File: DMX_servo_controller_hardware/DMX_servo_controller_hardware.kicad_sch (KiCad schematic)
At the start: 21 parts

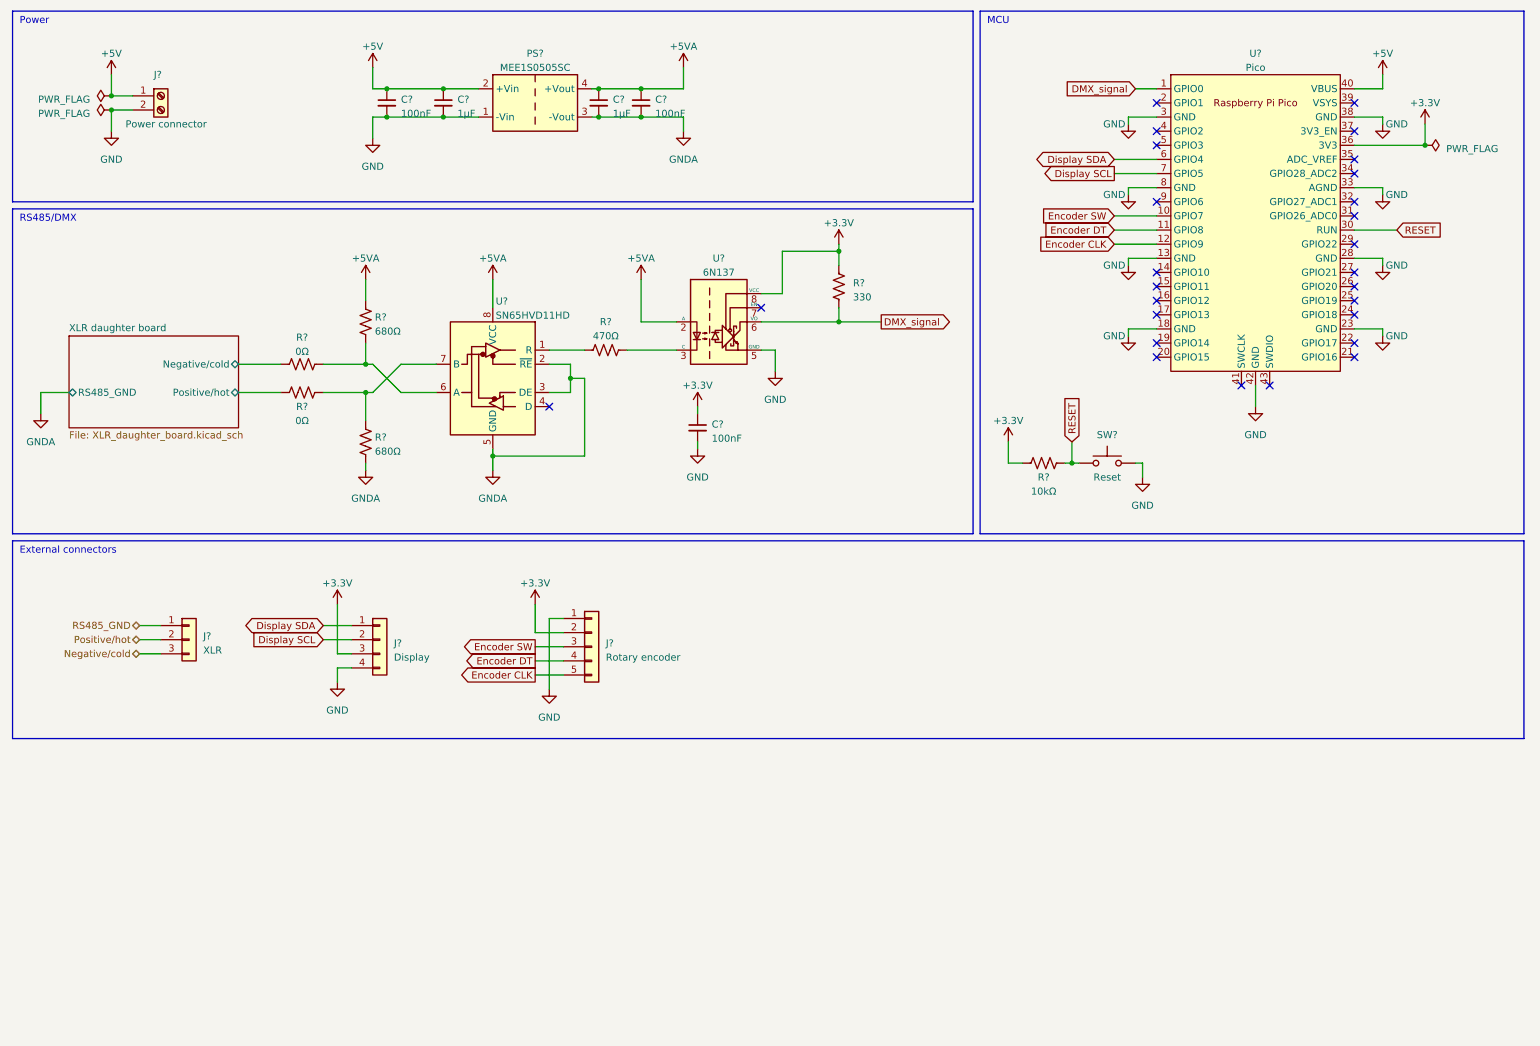
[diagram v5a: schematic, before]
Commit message: WIP: Adds PCA9685 PWM driver
This adds the IC and some minimal circuitry around it, but there's still
work to be done here.
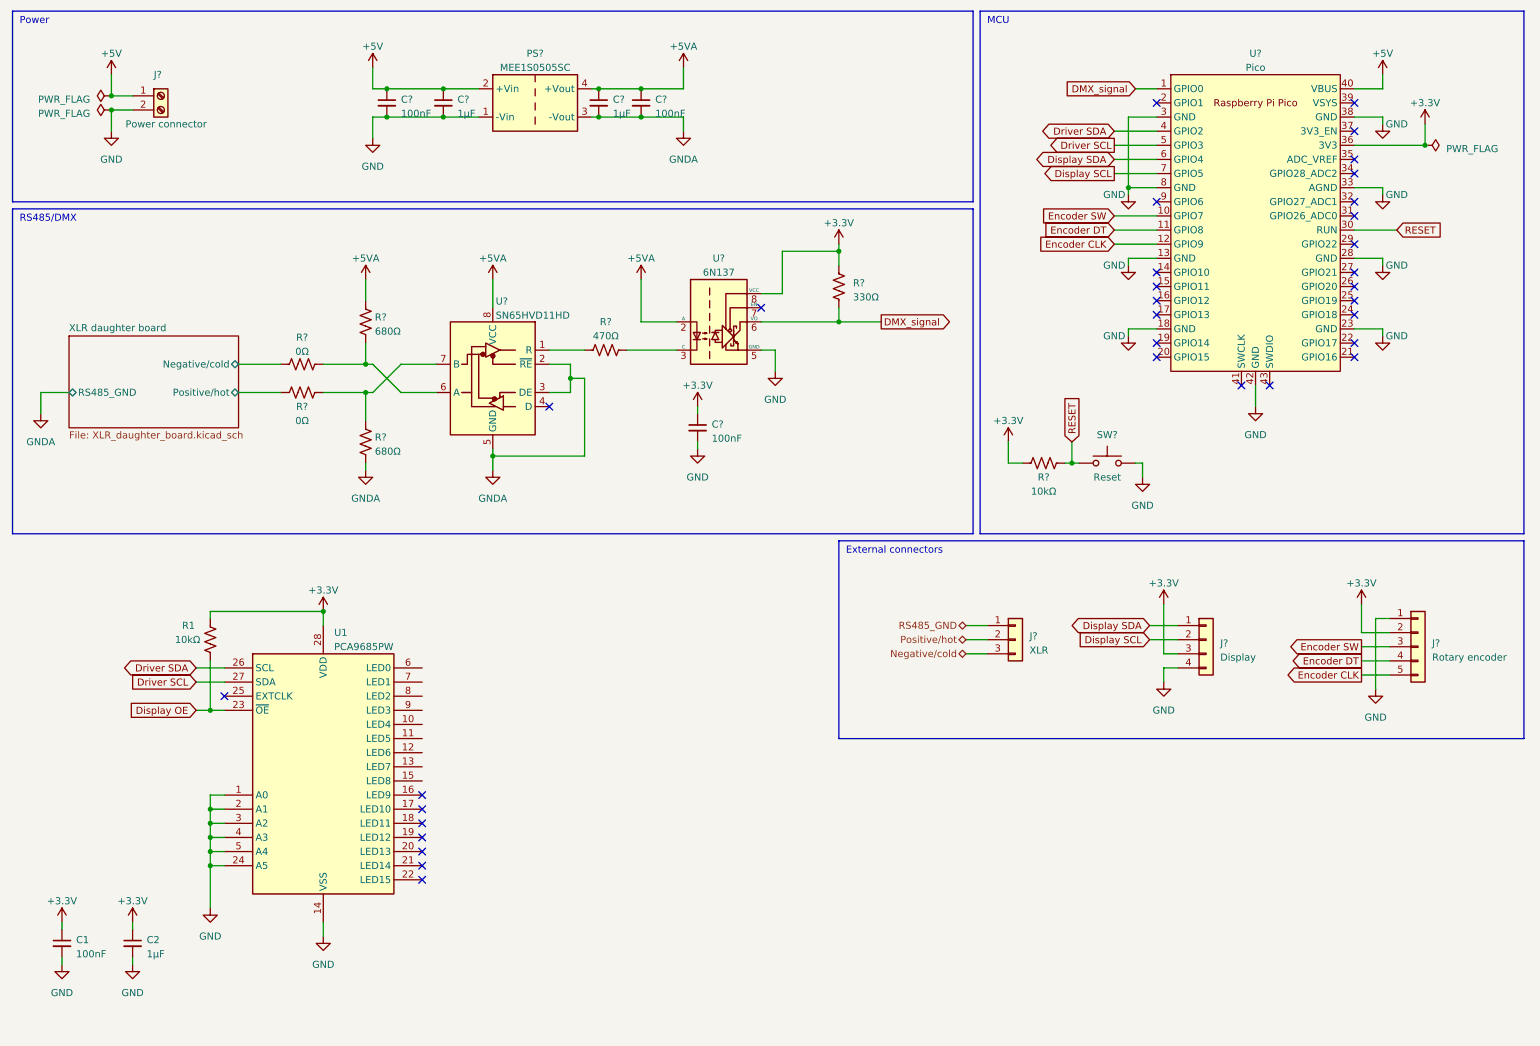
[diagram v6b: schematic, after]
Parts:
- added C1: 100nF, symbol Device:C_Small
- added C2: 1μF, symbol Device:C_Small
- added R1: 10kΩ, symbol Device:R_US
- added U1: PCA9685PW, Package_SO:TSSOP-28_4.4x9.7mm_P0.65mm, symbol Driver_LED:PCA9685PW
- R?: value 330 -> 330Ω
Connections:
- net +3.3V: now also C1.1, C2.1, R1.1, U1.28 (VDD)
- net GND: now also C1.2, C2.2, U1.1 (A0), U1.14 (VSS), U1.2 (A1), U1.24 (A5), U1.3 (A2), U1.4 (A3), U1.5 (A4)
- net Driver SDA: now reaches U?.4 (GPIO2)
- net Driver SDA: now also U1.26 (SCL)
- net Driver SCL: now reaches U?.5 (GPIO3)
- net Driver SCL: now also U1.27 (SDA)
- new net Display OE: R1.2, U1.23 (~{OE})
- no-connect marks 27 -> 33
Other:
- moved on the sheet: J?

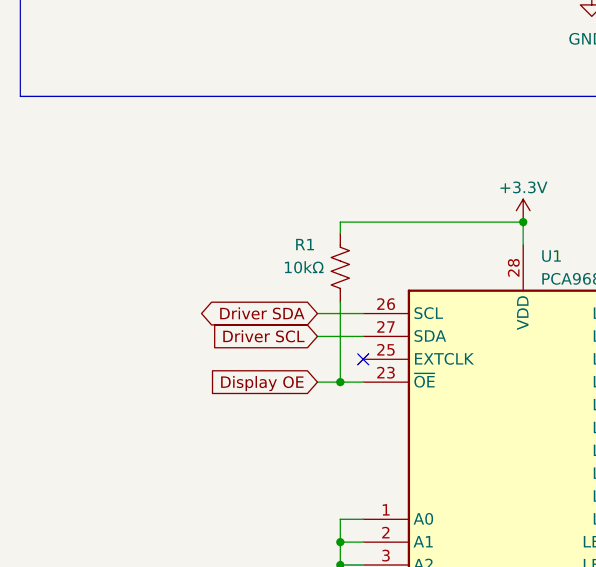
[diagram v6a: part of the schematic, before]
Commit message: Adds pull-up resistors to PCA9685 i2c lines
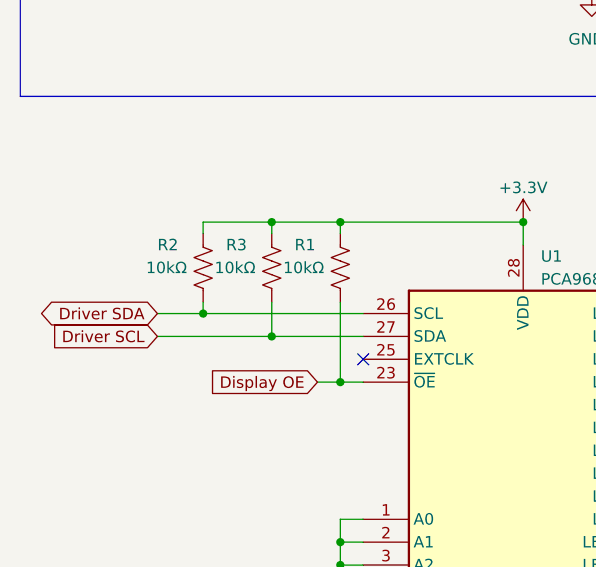
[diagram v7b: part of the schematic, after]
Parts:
- added R2, R3: 10kΩ, symbol Device:R_US
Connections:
- net +3.3V: now also R2.1, R3.1
- net Driver SCL: now also R3.2
- net Driver SDA: now also R2.2
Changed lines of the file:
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@@
   (junction (at 203.2 93.98) (diameter 0) (color 0 0 0 0)
   )
+  (junction (at 48.26 120.65) (diameter 0) (color 0 0 0 0)
+  )
   (junction (at 48.26 138.43) (diameter 0) (color 0 0 0 0)
   )
@@
   (junction (at 48.26 158.75) (diameter 0) (color 0 0 0 0)
   )
+  (junction (at 40.64 120.65) (diameter 0) (color 0 0 0 0)
+  )
   (junction (at 161.29 55.88) (diameter 0) (color 0 0 0 0)
   )
@@
   (junction (at 76.2 76.2) (diameter 0) (color 0 0 0 0)
   )
+  (junction (at 33.02 130.81) (diameter 0) (color 0 0 0 0)
+  )
   (junction (at 48.26 156.21) (diameter 0) (color 0 0 0 0)
   )
@@
   )
   (junction (at 80.01 26.67) (diameter 0) (color 0 0 0 0)
+  )
+  (junction (at 40.64 133.35) (diameter 0) (color 0 0 0 0)
   )
   (junction (at 125.73 26.67) (diameter 0) (color 0 0 0 0)
@@
   (no_connect (at 254 39.37))
   (no_connect (at 218.44 29.21))
+  (wire (pts (xy 40.64 120.65) (xy 48.26 120.65))
+    (stroke (width 0) (type default))
+  )
   (wire (pts (xy 210.82 39.37) (xy 218.44 39.37))
     (stroke (width 0) (type default))
@@
     (stroke (width 0) (type default))
   )
+  (wire (pts (xy 33.02 130.81) (xy 50.8 130.81))
+    (stroke (width 0) (type default))
+  )
   (wire (pts (xy 215.9 93.98) (xy 215.9 96.52))
     (stroke (width 0) (type default))
@@
     (stroke (width 0) (type default))
   )
+  (wire (pts (xy 33.02 130.81) (xy 33.02 129.54))
+    (stroke (width 0) (type default))
+  )
   (wire (pts (xy 210.82 54.61) (xy 218.44 54.61))
     (stroke (width 0) (type default))
@@
     (stroke (width 0) (type default))
   )
-  (wire (pts (xy 45.72 130.81) (xy 50.8 130.81))
+  (wire (pts (xy 27.94 130.81) (xy 33.02 130.81))
     (stroke (width 0) (type default))
   )
@@
     (stroke (width 0) (type default))
   )
+  (wire (pts (xy 33.02 120.65) (xy 40.64 120.65))
+    (stroke (width 0) (type default))
+  )
   (wire (pts (xy 254 69.85) (xy 259.08 69.85))
     (stroke (width 0) (type default))
@@
     (stroke (width 0) (type default))
   )
+  (wire (pts (xy 33.02 121.92) (xy 33.02 120.65))
+    (stroke (width 0) (type default))
+  )
   (wire (pts (xy 82.55 81.28) (xy 88.9 81.28))
     (stroke (width 0) (type default))
@@
     (stroke (width 0) (type default))
   )
-  (wire (pts (xy 45.72 133.35) (xy 50.8 133.35))
+  (wire (pts (xy 40.64 121.92) (xy 40.64 120.65))
+    (stroke (width 0) (type default))
+  )
+  (wire (pts (xy 27.94 133.35) (xy 40.64 133.35))
     (stroke (width 0) (type default))
   )
@@
   )
   (wire (pts (xy 161.29 68.58) (xy 161.29 66.04))
+    (stroke (width 0) (type default))
+  )
+  (wire (pts (xy 40.64 133.35) (xy 50.8 133.35))
+    (stroke (width 0) (type default))
+  )
+  (wire (pts (xy 40.64 129.54) (xy 40.64 133.35))
     (stroke (width 0) (type default))
   )
@@
     )
   )
-  (global_label "Driver SDA" (shape bidirectional) (at 45.72 130.81 180) (fields_autoplaced)
-    (effects (font (size 1.27 1.27)) (justify right))
-    (property "Intersheetrefs" "${INTERSHEET_REFS}" (at 31.6638 130.81 0)
+  (global_label "Driver SDA" (shape bidirectional) (at 27.94 130.81 180) (fields_autoplaced)
+    (effects (font (size 1.27 1.27)) (justify right))
+    (property "Intersheetrefs" "${INTERSHEET_REFS}" (at 13.8838 130.81 0)
       (effects (font (size 1.27 1.27)) (justify right) hide)
     )
@@
     )
   )
-  (global_label "Driver SCL" (shape input) (at 45.72 133.35 180) (fields_autoplaced)
-    (effects (font (size 1.27 1.27)) (justify right))
-    (property "Intersheetrefs" "${INTERSHEET_REFS}" (at 32.8356 133.35 0)
+  (global_label "Driver SCL" (shape input) (at 27.94 133.35 180) (fields_autoplaced)
+    (effects (font (size 1.27 1.27)) (justify right))
+    (property "Intersheetrefs" "${INTERSHEET_REFS}" (at 15.0556 133.35 0)
       (effects (font (size 1.27 1.27)) (justify right) hide)
     )
@@
         (path "/cd90393c-7fb4-4867-84b8-7df1a2bf6613"
           (reference "#PWR?") (unit 1)
+        )
+      )
+    )
+  )
+  (symbol (lib_id "Device:R_US") (at 40.64 125.73 0) (unit 1)
+    (in_bom yes) (on_board yes) (dnp no)
+    (property "Reference" "R3" (at 35.56 123.19 0)
+      (effects (font (size 1.27 1.27)) (justify left))
+    )
+    (property "Value" "10kΩ" (at 34.29 125.73 0)
+      (effects (font (size 1.27 1.27)) (justify left))
+    )
+    (property "Footprint" "" (at 41.656 125.984 90)
+      (effects (font (size 1.27 1.27)) hide)
+    )
+    (property "Datasheet" "~" (at 40.64 125.73 0)
+      (effects (font (size 1.27 1.27)) hide)
+    )
+    (pin "1")
+    (pin "2")
+    (instances
+      (project "DMX_servo_controller_hardware"
+        (path "/cd90393c-7fb4-4867-84b8-7df1a2bf6613"
+          (reference "R3") (unit 1)
         )
       )
@@
         )
       )
+    )
+  )
+  (symbol (lib_id "Device:R_US") (at 33.02 125.73 0) (unit 1)
+    (in_bom yes) (on_board yes) (dnp no)
+    (property "Reference" "R2" (at 27.94 123.19 0)
+      (effects (font (size 1.27 1.27)) (justify left))
+    )
+    (property "Value" "10kΩ" (at 26.67 125.73 0)
+      (effects (font (size 1.27 1.27)) (justify left))
+    )
+    (property "Footprint" "" (at 34.036 125.984 90)
+      (effects (font (size 1.27 1.27)) hide)
+    )
+    (property "Datasheet" "~" (at 33.02 125.73 0)
+      (effects (font (size 1.27 1.27)) hide)
+    )
+    (pin "1")
+    (pin "2")
+    (instances
+      (project "DMX_servo_controller_hardware"
+        (path "/cd90393c-7fb4-4867-84b8-7df1a2bf6613"
+          (reference "R2") (unit 1)
+        )
+      )

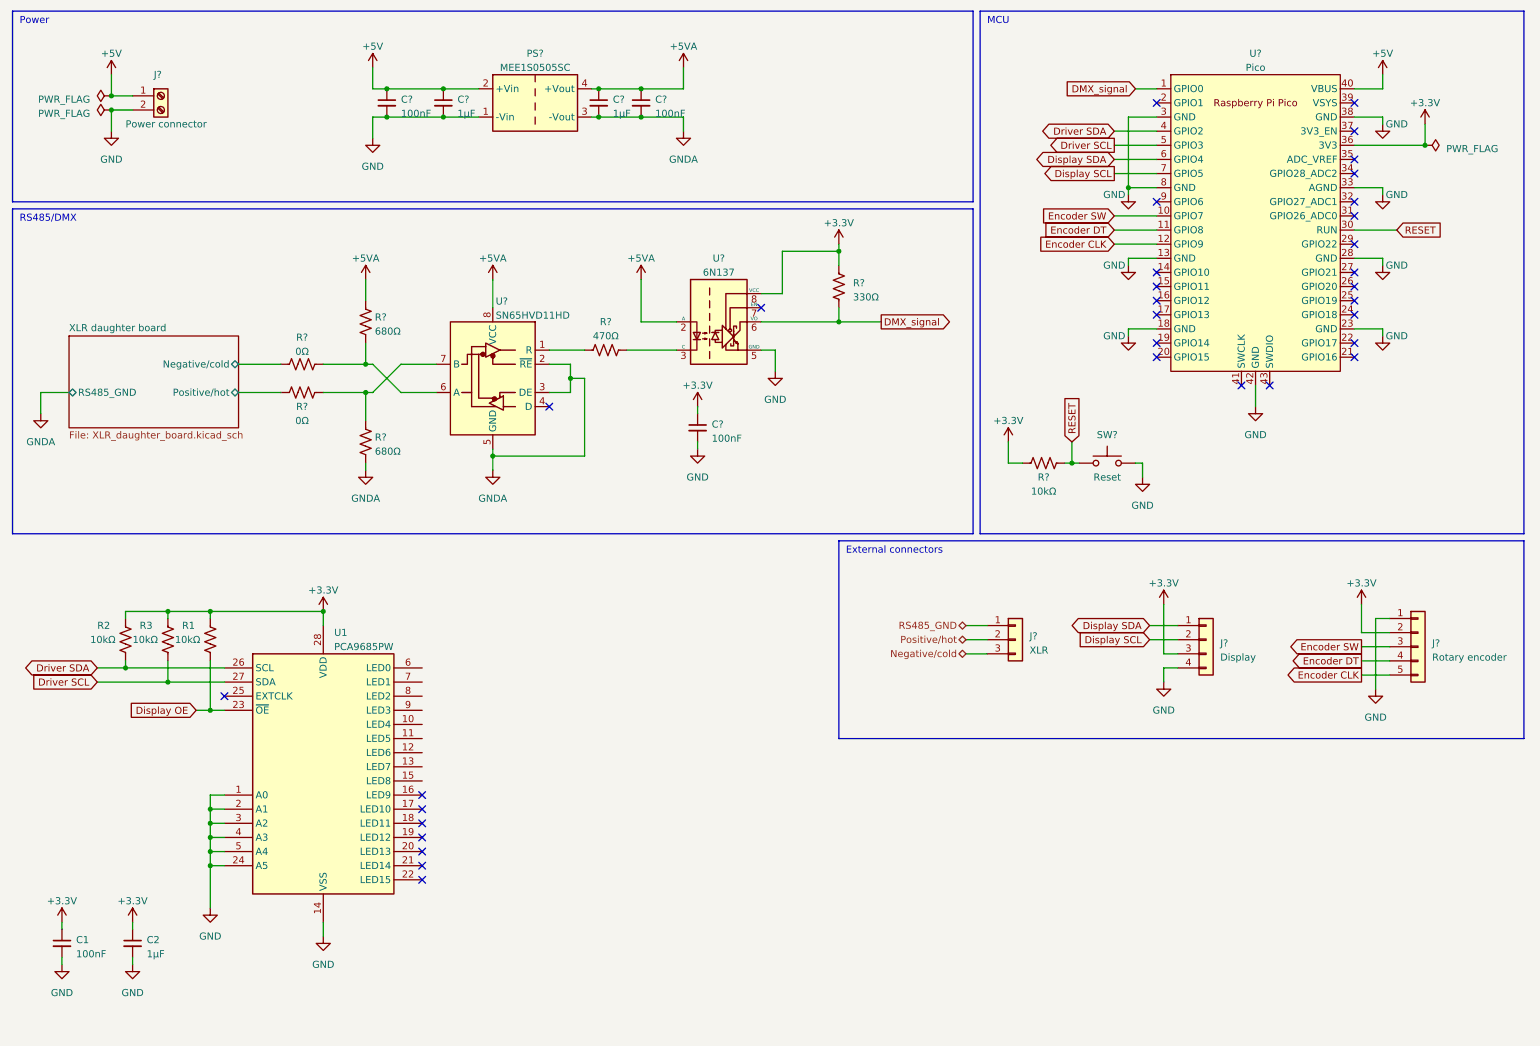
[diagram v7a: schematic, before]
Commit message: Adds external connectors for the servos
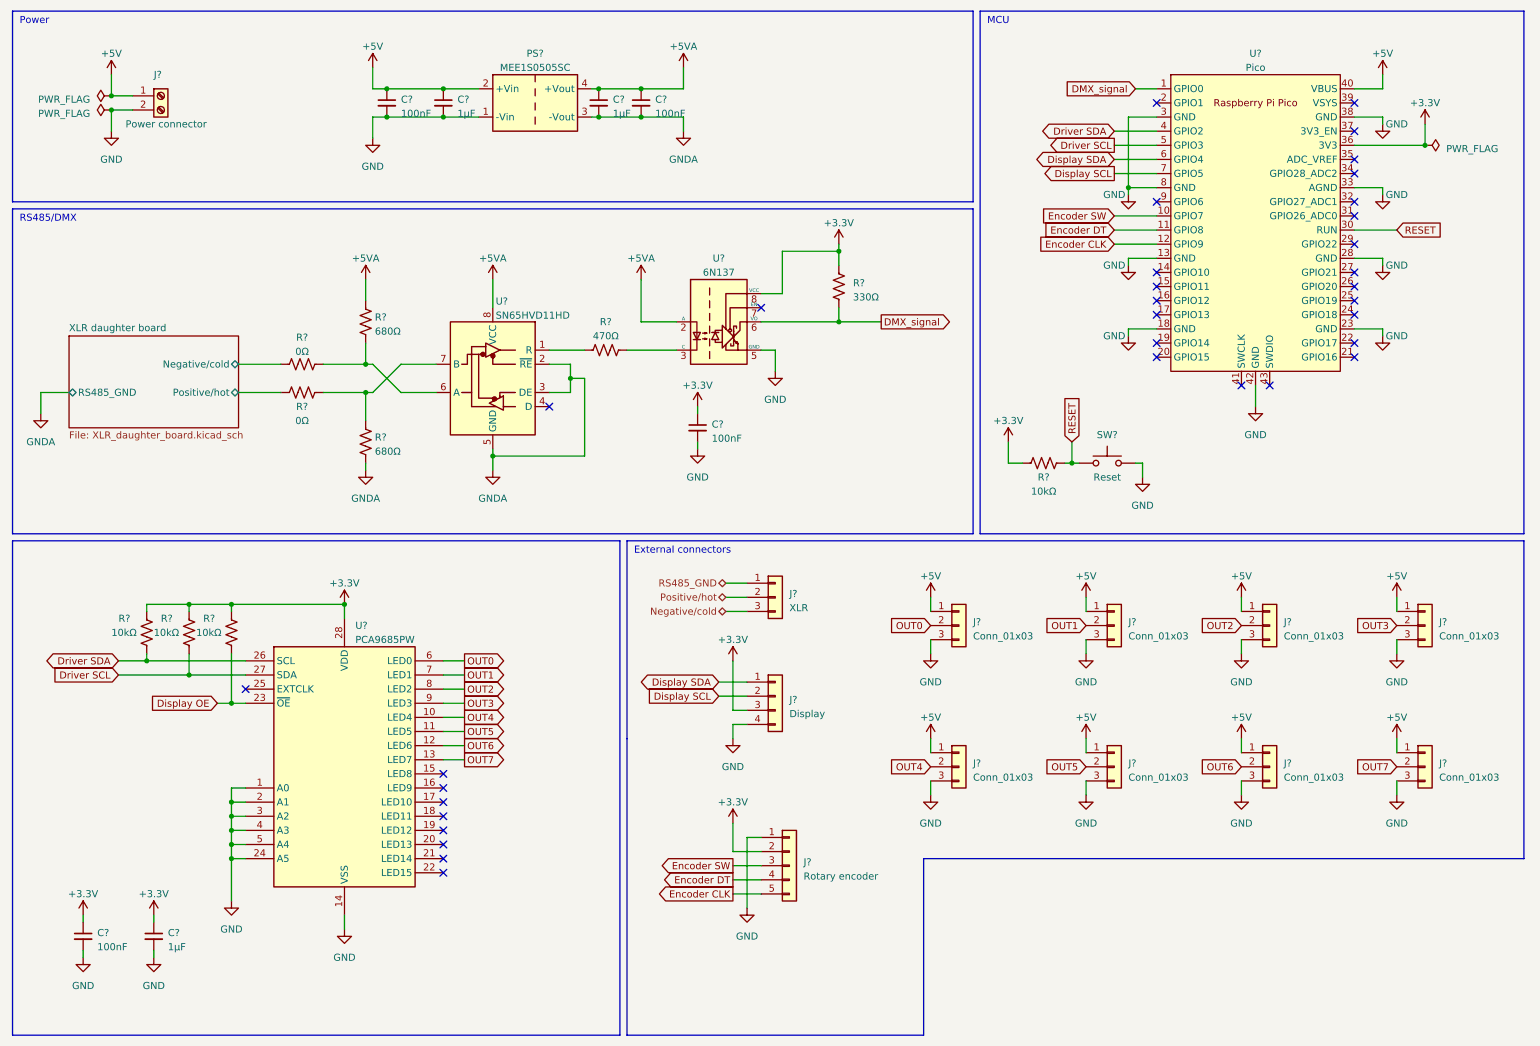
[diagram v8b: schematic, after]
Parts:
- added J? (x8): Conn_01x03, symbol Connector_Generic:Conn_01x03
- renumbered C1 to C?, C2 to C?, R3 to R?, R2 to R?, R1 to R?, U1 to U?
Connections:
- net +5V: now also J?.1 (Pin_1), J?.1 (Pin_1), J?.1 (Pin_1), J?.1 (Pin_1), J?.1 (Pin_1), J?.1 (Pin_1), J?.1 (Pin_1), J?.1 (Pin_1)
- net GND: now also J?.3 (Pin_3), J?.3 (Pin_3), J?.3 (Pin_3), J?.3 (Pin_3), J?.3 (Pin_3), J?.3 (Pin_3), J?.3 (Pin_3), J?.3 (Pin_3)
- net OUT4: now reaches U?.10 (LED4)
- net OUT4: now also J?.2 (Pin_2)
- net OUT5: now reaches U?.11 (LED5)
- net OUT5: now also J?.2 (Pin_2)
- net OUT6: now reaches U?.12 (LED6)
- net OUT6: now also J?.2 (Pin_2)
- net OUT7: now reaches U?.13 (LED7)
- net OUT7: now also J?.2 (Pin_2)
- net OUT0: now reaches U?.6 (LED0)
- net OUT0: now also J?.2 (Pin_2)
- net OUT1: now reaches U?.7 (LED1)
- net OUT1: now also J?.2 (Pin_2)
- net OUT2: now reaches U?.8 (LED2)
- net OUT2: now also J?.2 (Pin_2)
- net OUT3: now reaches U?.9 (LED3)
- net OUT3: now also J?.2 (Pin_2)
- no-connect marks 33 -> 34
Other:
- moved on the sheet: C?, J?, R?, U?
